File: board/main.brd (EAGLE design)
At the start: 91 x 76 mm, 63 parts, among them J1 HEADER4VALULOK, J2 HEADER6, J3 FUSE, U2 INA181, U3 TC1240A, U4 K78U05, U5 DGD2304, U6 DGD2304, U7 DGD2304

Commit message: Pointone update
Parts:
- removed C10: 470uF, SparkFun-Capacitors:CPOL-RADIAL-5MM-10MM
- removed C6, C7, C8: 22nF, SparkFun-Capacitors:1206
- added R14, R15, R16, R17, R18, R19: 22, SparkFun-Resistors:1206
- moved D1 43.9 mm to (5.20, 46.2), turned to 180 degrees
- moved C4 23.3 mm to (45.0, 27.0), turned to 0 degrees
- moved R12 10.0 mm to (40.0, 13.0), turned to 0 degrees
- moved R13 10.0 mm to (40.0, 16.0), turned to 180 degrees
- moved U4 8.94 mm to (44.0, 4.00), turned to 180 degrees
- moved C12 7.07 mm to (16.0, 13.0)
- moved C13 6.40 mm to (16.0, 9.00)
- moved C5 6.02 mm to (45.0, 40.0), turned to 0 degrees
- moved C19 5.02 mm to (50.0, 52.0)
- moved U3 5.00 mm to (23.0, 11.0), turned to 0 degrees
- moved C14 3.61 mm to (30.0, 13.0), turned to 180 degrees
- moved C18 3.16 mm to (30.0, 9.00)
- moved C11 3.00 mm to (30.0, 5.00)
- moved R4 3.00 mm to (82.0, 44.0)
- moved R5 3.00 mm to (85.0, 44.0)
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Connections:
- new net N$11: Q2.4, R15.2
- new net N$13: Q3.4, R16.2
- new net N$14: Q4.4, R17.2
- new net N$15: Q5.4, R18.2
- new net N$16: Q6.4, R19.2
- new net N$5: Q1.4, R14.2
- net DRV_AH: now also R14.1; no longer Q1.4
- net DRV_AL: now also R15.1; no longer Q2.4
- net DRV_BH: now also R16.1; no longer Q3.4
- net DRV_BL: now also R17.1; no longer Q4.4
- net DRV_CH: now also R18.1; no longer Q5.4
- net DRV_CL: now also R19.1; no longer Q6.4
- net GND: no longer C10.-, C6.2, C7.2, C8.2
- net HALL_A: no longer C6.1
- net HALL_B: no longer C7.1
- net HALL_C: no longer C8.1
- net V_RAW: no longer C10.+
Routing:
- net DRV_CL: track 37.3 -> 3.98 mm, vias 2 -> 0
- net DRV_AL: track 36.6 -> 3.82 mm, vias 2 -> 0
- net DRV_BL: track 35.6 -> 3.98 mm, vias 2 -> 0
- net N$16: track 0.00 -> 29.3 mm, vias 0 -> 2
- net N$14: track 0.00 -> 28.0 mm, vias 0 -> 2
- net N$11: track 0.00 -> 27.2 mm, vias 0 -> 2
- net DRV_AH: track 32.3 -> 8.39 mm, vias 2 -> 0
- net DRV_CH: track 31.8 -> 8.81 mm, vias 2 -> 0
- net DRV_BH: track 30.8 -> 8.81 mm, vias 2 -> 0
- net N$15: track 0.00 -> 18.9 mm, vias 0 -> 2
- net V_RAW: track 52.6 -> 33.7 mm, vias 2 -> 1
- net N$5: track 0.00 -> 18.5 mm, vias 0 -> 2
- net N$13: track 0.00 -> 17.7 mm, vias 0 -> 2
- net VSENSE: track 11.6 -> 24.8 mm, vias 0 -> 2
- net CTRL_CH: track 24.8 -> 37.4 mm
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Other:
- board text added: "EasyController3.1 Designed by PLG, July 2023 Shell Eco-Marathon"
- board text removed: "EasyController3.0 Designed by PLG, March 2023 Shell Eco-Marathon"

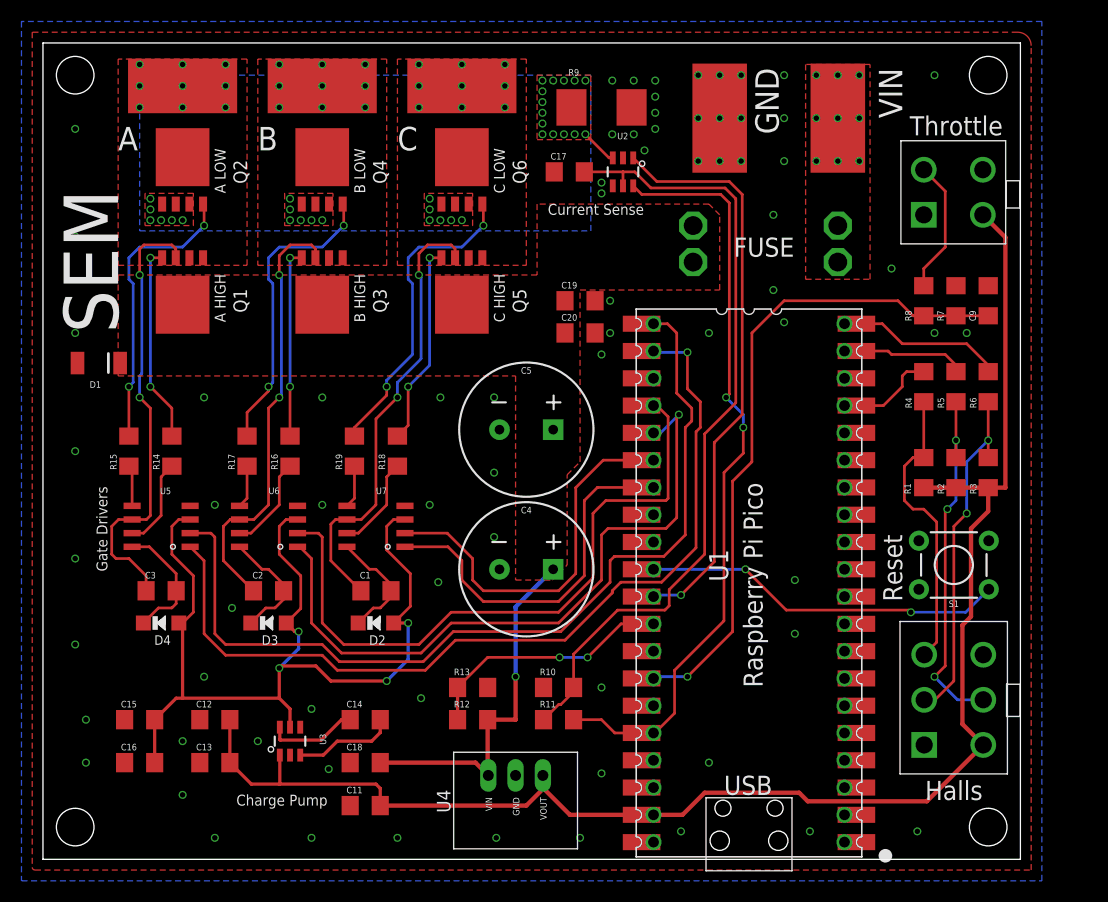
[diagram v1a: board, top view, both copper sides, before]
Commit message: 3.2 initial commit, changed FETs to TO-220s
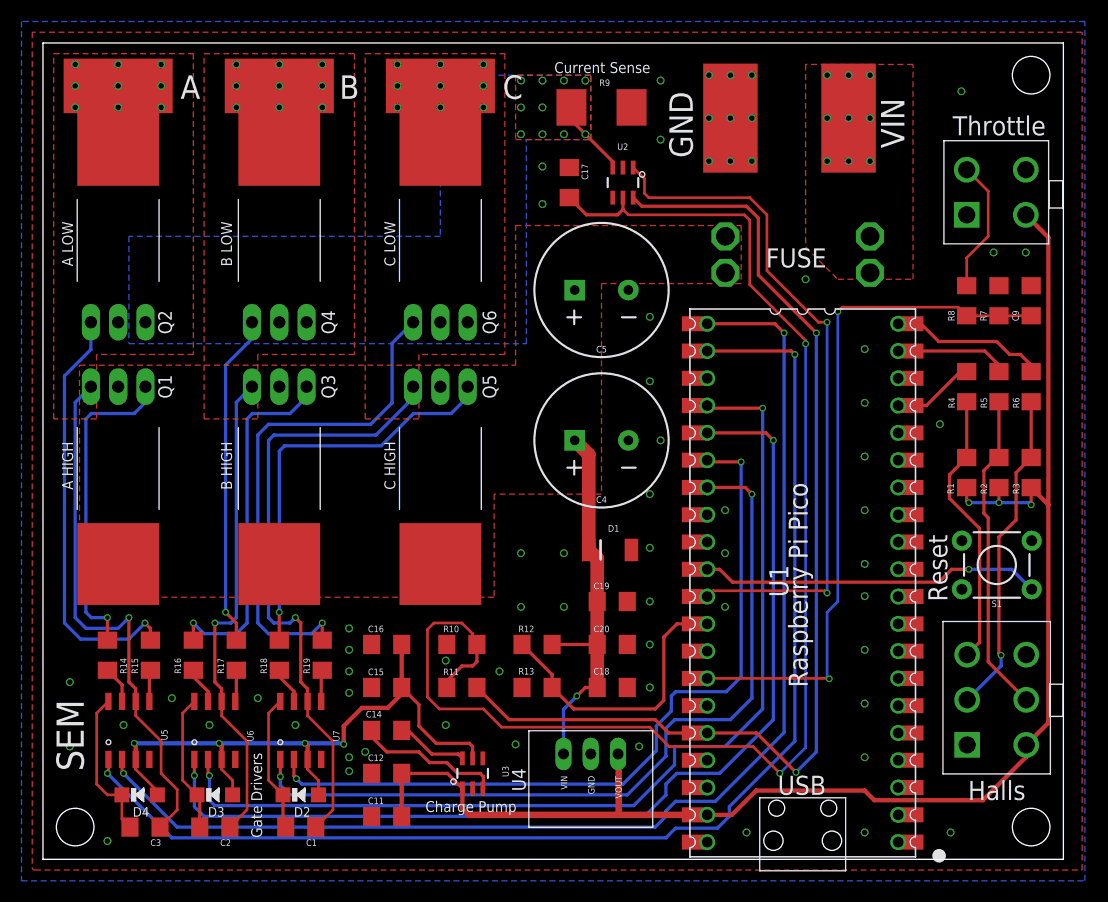
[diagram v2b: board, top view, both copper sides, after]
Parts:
- removed C13: 1uF, SparkFun-Capacitors:1206
- removed U$13: SCREW, Custom_old:M3HOLE
- Q1, Q2, Q3, Q4, Q5, Q6: value (none) -> MOSFET-NCHANNELTO-220-FLAT; device 2018:DFN5X6 -> Custom_old:TO-220-FLAT
- moved D1 50.7 mm to (52.8, 28.8), turned to 0 degrees
- moved C20 29.2 mm to (53.0, 20.0)
- moved C19 28.2 mm to (53.0, 24.0)
- moved C16 25.5 mm to (32.0, 20.0)
- moved C18 24.0 mm to (53.0, 16.0), turned to 0 degrees
- moved C15 23.2 mm to (32.0, 16.0)
- moved C1 23.1 mm to (24.0, 3.00), turned to 0 degrees
- moved C2 22.6 mm to (16.0, 3.00), turned to 0 degrees
- moved C3 22.1 mm to (9.50, 3.00), turned to 0 degrees
- moved R18 22.0 mm to (22.0, 19.0)
- moved R16 21.0 mm to (14.0, 19.0)
- moved U7 20.2 mm to (24.0, 12.0), turned to 90 degrees
- moved R14 19.9 mm to (6.00, 19.0)
- moved U6 19.6 mm to (16.0, 12.0), turned to 90 degrees
- moved R19 19.2 mm to (26.0, 19.0)
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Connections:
- net 5V: no longer C13.1
- net COM_A: now also Q2.2; no longer Q1.1, Q1.2
- net COM_B: now also Q4.2; no longer Q3.1, Q3.2
- net COM_C: now also Q6.2; no longer Q5.1, Q5.2
- net GND: no longer C13.2
- net N$11: now also Q2.1; no longer Q2.4
- net N$13: now also Q3.1; no longer Q3.4
- net N$14: now also Q4.1; no longer Q4.4
- net N$15: now also Q5.1; no longer Q5.4
- net N$16: now also Q6.1; no longer Q6.4
- net N$5: now also Q1.1; no longer Q1.4
- net SHUNT+: no longer Q2.1, Q2.2, Q4.1, Q4.2, Q6.1, Q6.2
- net V_RAW: now also Q1.2, Q3.2, Q5.2
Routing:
- net N$10: track 75.0 -> 127.6 mm, vias 0 -> 2
- net CTRL_CL: track 35.9 -> 76.5 mm, vias 0 -> 2
- net CTRL_CH: track 37.4 -> 74.2 mm, vias 0 -> 2
- net CTRL_AL: track 83.9 -> 117.5 mm, vias 1 -> 2
- net CTRL_BL: track 64.4 -> 96.5 mm, vias 1 -> 2
- net CTRL_BH: track 63.1 -> 94.7 mm, vias 0 -> 2
- net 10V: track 90.8 -> 60.0 mm
- net CTRL_AH: track 85.6 -> 114.7 mm, vias 0 -> 2
- net 3.3V: track 72.3 -> 101.1 mm
- net N$15: track 18.9 -> 38.2 mm, vias 2 -> 1
- net N$16: track 29.3 -> 48.0 mm, vias 2 -> 1
- net N$13: track 17.7 -> 33.8 mm, vias 2 -> 1
- net COM_C: track 42.2 -> 57.2 mm, vias 11 -> 10
- net N$11: track 27.2 -> 39.6 mm, vias 2 -> 1
- net N$5: track 18.5 -> 29.9 mm, vias 2 -> 1
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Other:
- board size 91 x 76 mm -> 95 x 76 mm
- board text added: "EasyController3.2 Designed by PLG, Dec 2023 Shell Eco-Marathon"
- board text removed: "EasyController3.1 Designed by PLG, July 2023 Shell Eco-Marathon"

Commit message: Code works
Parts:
- Q1, Q2, Q3, Q4, Q5, Q6: value MOSFET-NCHANNELTO-220-FLAT -> (none)
- R9: value 0.001 -> 0.0005
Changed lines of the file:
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@@
 <attribute name="VALUE" x="23" y="1.857" size="0.6096" layer="27" font="vector" ratio="20" align="top-center"/>
 </element>
-<element name="Q1" library="Custom_old" package="TO-220-FLAT" value="MOSFET-NCHANNELTO-220-FLAT" x="7" y="44" smashed="yes" rot="R180">
+<element name="Q1" library="Custom_old" package="TO-220-FLAT" value="" x="7" y="44" smashed="yes" rot="R180">
 <attribute name="NAME" x="12" y="44" size="1.27" layer="25" rot="R90" align="bottom-center"/>
 </element>
-<element name="Q2" library="Custom_old" package="TO-220-FLAT" value="MOSFET-NCHANNELTO-220-FLAT" x="7" y="50" smashed="yes">
+<element name="Q2" library="Custom_old" package="TO-220-FLAT" value="" x="7" y="50" smashed="yes">
 <attribute name="NAME" x="12" y="50" size="1.27" layer="25" rot="R90" align="bottom-center"/>
 </element>
 <element name="U$4" library="Custom_old" package="PAD" value="PAD" x="75" y="69" smashed="yes" rot="R90"/>
 <element name="U$5" library="Custom_old" package="PAD" value="PAD" x="64" y="69" smashed="yes" rot="R270"/>
-<element name="Q3" library="Custom_old" package="TO-220-FLAT" value="MOSFET-NCHANNELTO-220-FLAT" x="22" y="44" smashed="yes" rot="R180">
+<element name="Q3" library="Custom_old" package="TO-220-FLAT" value="" x="22" y="44" smashed="yes" rot="R180">
 <attribute name="NAME" x="27.2" y="44" size="1.27" layer="25" rot="R90" align="bottom-center"/>
 </element>
-<element name="Q4" library="Custom_old" package="TO-220-FLAT" value="MOSFET-NCHANNELTO-220-FLAT" x="22" y="50" smashed="yes">
+<element name="Q4" library="Custom_old" package="TO-220-FLAT" value="" x="22" y="50" smashed="yes">
 <attribute name="NAME" x="27.2" y="50" size="1.27" layer="25" rot="R90" align="bottom-center"/>
 </element>
-<element name="Q5" library="Custom_old" package="TO-220-FLAT" value="MOSFET-NCHANNELTO-220-FLAT" x="37" y="44" smashed="yes" rot="R180">
+<element name="Q5" library="Custom_old" package="TO-220-FLAT" value="" x="37" y="44" smashed="yes" rot="R180">
 <attribute name="NAME" x="42.2" y="44" size="1.27" layer="25" rot="R90" align="bottom-center"/>
 </element>
-<element name="Q6" library="Custom_old" package="TO-220-FLAT" value="MOSFET-NCHANNELTO-220-FLAT" x="37" y="50" smashed="yes">
+<element name="Q6" library="Custom_old" package="TO-220-FLAT" value="" x="37" y="50" smashed="yes">
 <attribute name="NAME" x="42.2" y="50" size="1.27" layer="25" rot="R90" align="bottom-center"/>
 </element>
@@
 <element name="D2" library="Seeed-Diode" package="SOD-123" value="" x="24" y="6" smashed="yes" rot="R180">
 <attribute name="MPN" value="MMSD4148" x="24" y="6" size="1.778" layer="27" rot="R180" display="off"/>
+<attribute name="NAME" x="24.905" y="4.857" size="0.889" layer="25" ratio="11" rot="R180"/>
 <attribute name="NAME" x="24.889" y="6.635" size="0.381" layer="33" ratio="10" rot="R180"/>
-<attribute name="NAME" x="24.905" y="4.857" size="0.889" layer="25" ratio="11" rot="R180"/>
 <attribute name="VALUE" x="25.905" y="8.032" size="0.889" layer="27" font="vector" ratio="11" rot="R180"/>
 </element>
@@
 <element name="D3" library="Seeed-Diode" package="SOD-123" value="" x="16" y="6" smashed="yes" rot="R180">
 <attribute name="MPN" value="MMSD4148" x="16" y="9" size="1.778" layer="27" rot="R180" display="off"/>
+<attribute name="NAME" x="16.889" y="6.635" size="0.381" layer="33" ratio="10" rot="R180"/>
 <attribute name="NAME" x="16.905" y="4.857" size="0.889" layer="25" ratio="11" rot="R180"/>
-<attribute name="NAME" x="16.889" y="6.635" size="0.381" layer="33" ratio="10" rot="R180"/>
 <attribute name="VALUE" x="17.905" y="8.032" size="0.889" layer="27" font="vector" ratio="11" rot="R180"/>
 </element>
@@
 <element name="D4" library="Seeed-Diode" package="SOD-123" value="" x="9" y="6" smashed="yes" rot="R180">
 <attribute name="MPN" value="MMSD4148" x="9" y="9" size="1.778" layer="27" rot="R180" display="off"/>
+<attribute name="NAME" x="9.889" y="6.635" size="0.381" layer="33" ratio="10" rot="R180"/>
 <attribute name="NAME" x="9.905" y="4.857" size="0.889" layer="25" ratio="11" rot="R180"/>
-<attribute name="NAME" x="9.889" y="6.635" size="0.381" layer="33" ratio="10" rot="R180"/>
 <attribute name="VALUE" x="10.905" y="8.032" size="0.889" layer="27" font="vector" ratio="11" rot="R180"/>
 </element>
@@
 <attribute name="VALUE" x="33" y="13.2" size="0.6096" layer="27" font="vector" ratio="20" align="bottom-center"/>
 </element>
-<element name="R9" library="Custom_old" package="R2512" value="0.001" x="52" y="70" smashed="yes" rot="R180">
+<element name="R9" library="Custom_old" package="R2512" value="0.0005" x="52" y="70" smashed="yes" rot="R180">
 <attribute name="NAME" x="52.8" y="72.6" size="0.6096" layer="25" rot="R180"/>
 <attribute name="VALUE" x="56" y="72.6" size="0.6096" layer="27" rot="R180"/>
@@
 <via x="65.5" y="2.5" extent="1-16" drill="0.5"/>
 <via x="76.5" y="2.5" extent="1-16" drill="0.5"/>
-<via x="76.5" y="9.5" extent="1-16" drill="0.5"/>
 <via x="84.5" y="2.5" extent="1-16" drill="0.5"/>
 <via x="55.5" y="10.5" extent="1-16" drill="0.5"/>
@@
 <via x="28.5" y="21.5" extent="1-16" drill="0.5"/>
 <via x="37.5" y="18.5" extent="1-16" drill="0.5"/>
-<via x="76.5" y="14.5" extent="1-16" drill="0.5"/>
 <via x="76.5" y="19.5" extent="1-16" drill="0.5"/>
 <via x="76.5" y="24.5" extent="1-16" drill="0.5"/>
